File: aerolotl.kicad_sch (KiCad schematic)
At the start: 0 parts

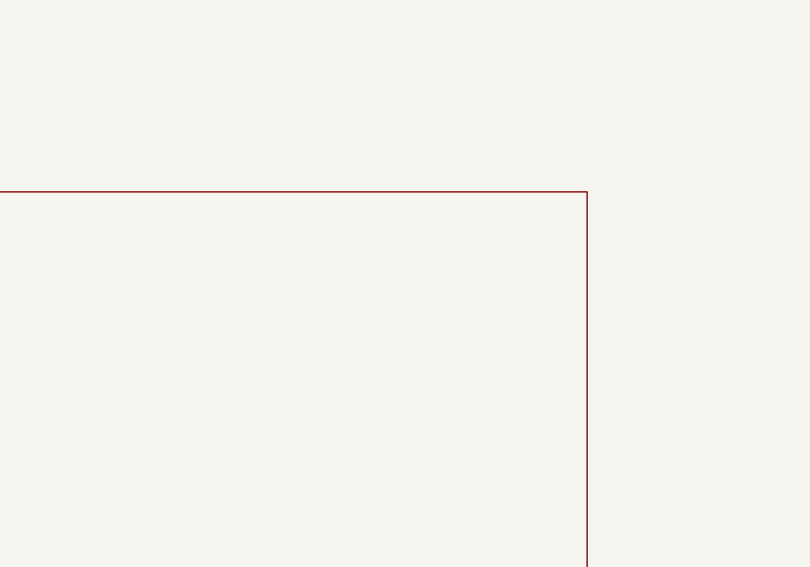
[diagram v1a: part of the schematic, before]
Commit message: Modified schematics for IMUs
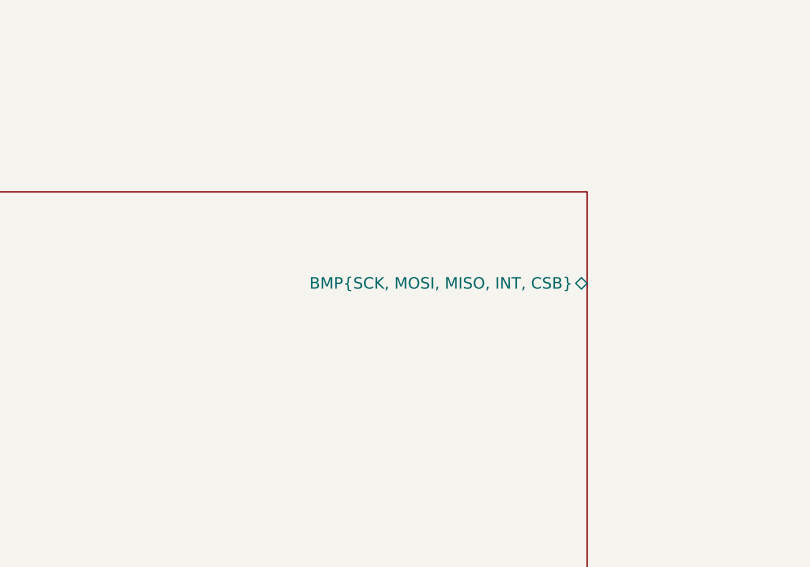
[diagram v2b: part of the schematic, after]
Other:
- sheet IMUs ports: added BMP{SCK, MOSI, MISO, INT, CSB}; removed none
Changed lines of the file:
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@@
+			)
+		)
+		(pin "BMP{SCK, MOSI, MISO, INT, CSB}" bidirectional
+			(at 104.14 218.44 0)
+			(effects
+				(font
+					(size 1.27 1.27)
+				)
+				(justify right)
 			)
 		)

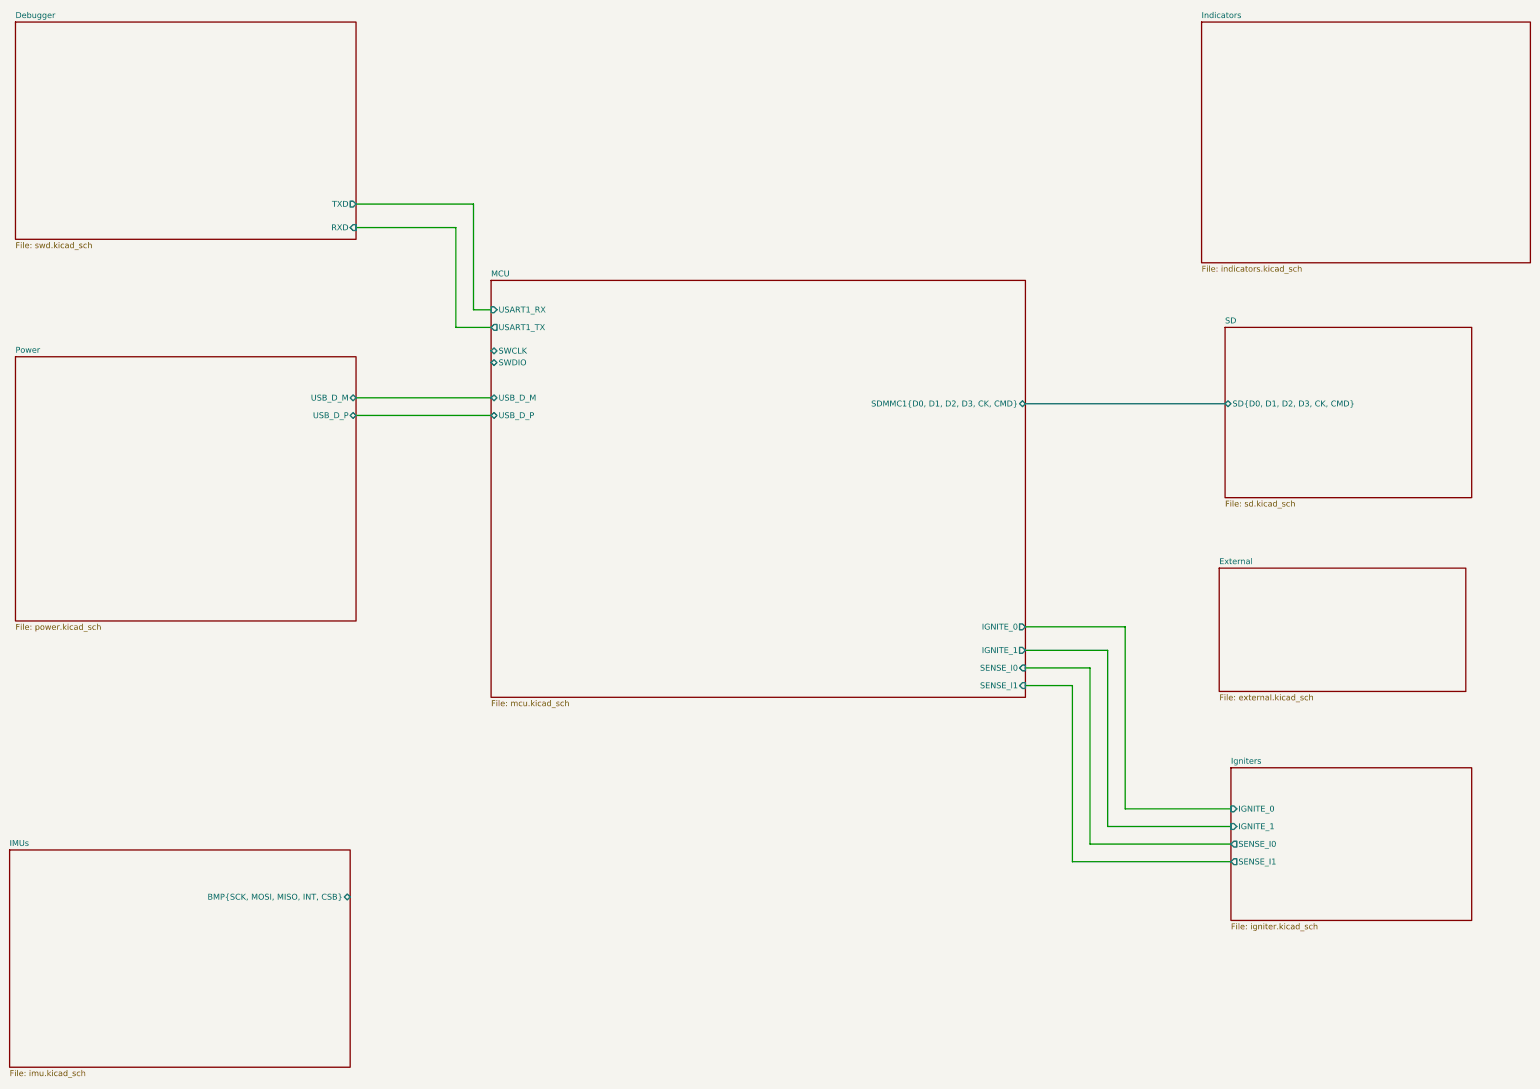
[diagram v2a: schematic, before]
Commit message: added current rush limiting resistors to bmp581
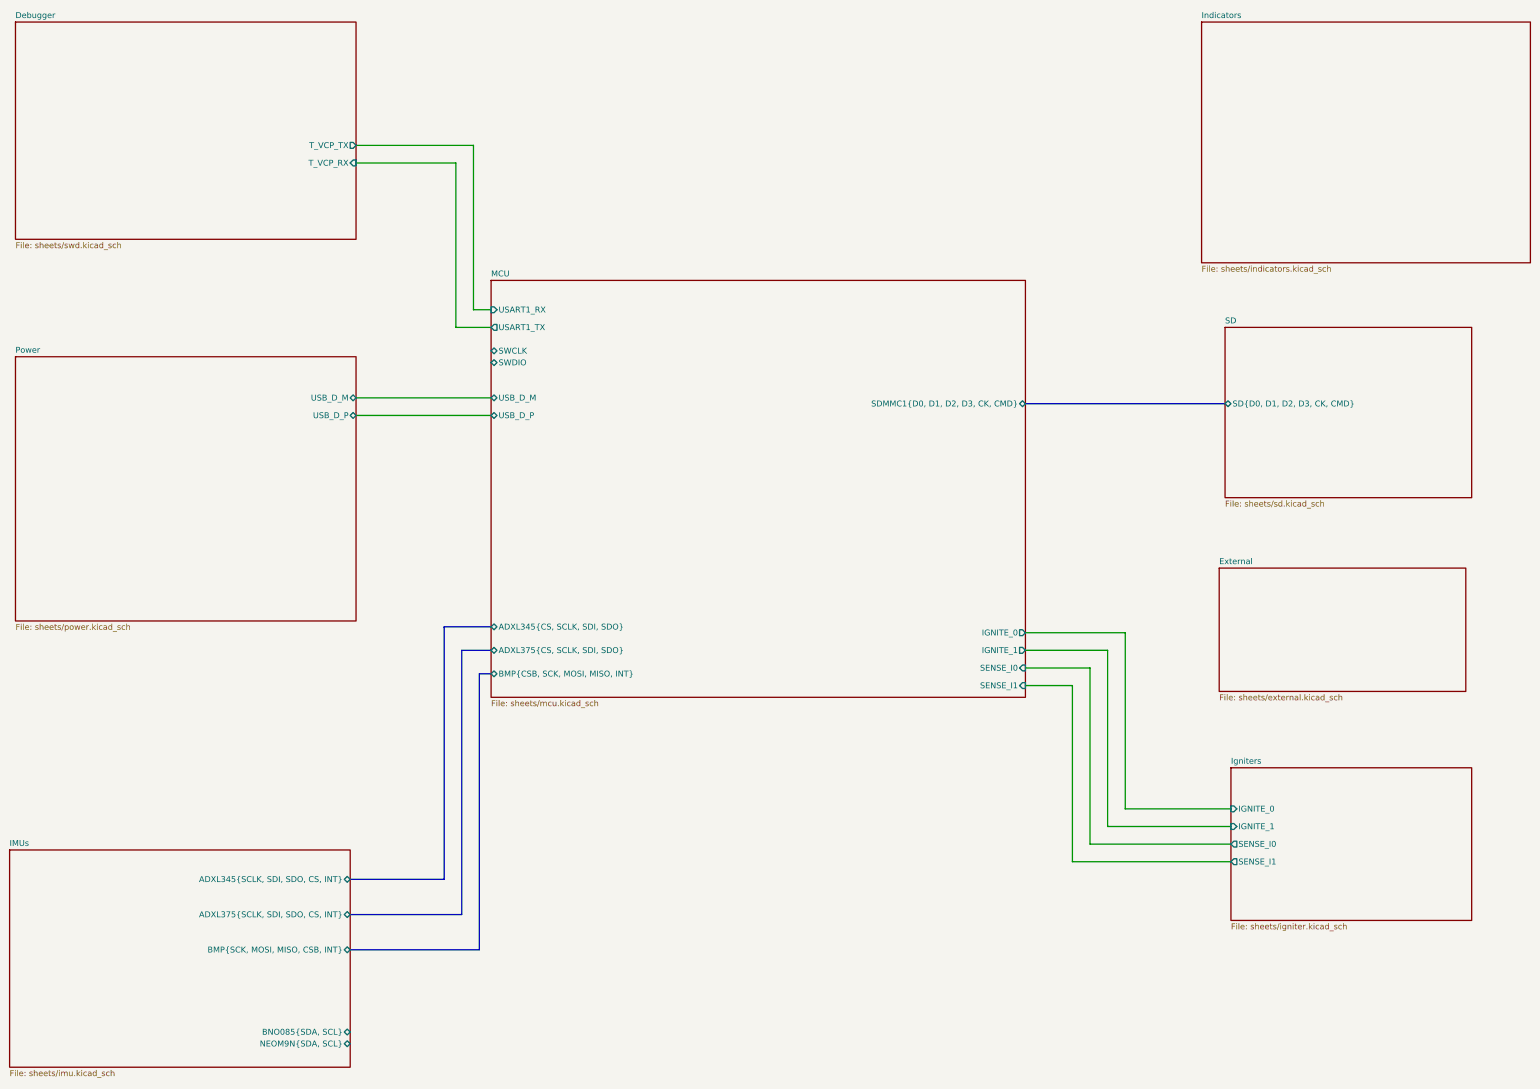
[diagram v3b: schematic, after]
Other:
- sheet Debugger: file swd.kicad_sch -> sheets/swd.kicad_sch
- sheet Debugger ports: added T_VCP_RX, T_VCP_TX; removed RXD, TXD
- sheet External: file external.kicad_sch -> sheets/external.kicad_sch
- sheet IMUs: file imu.kicad_sch -> sheets/imu.kicad_sch
- sheet IMUs ports: added ADXL345{SCLK, SDI, SDO, CS, INT}, ADXL375{SCLK, SDI, SDO, CS, INT}, BMP{SCK, MOSI, MISO, CSB, INT}, BNO085{SDA, SCL}, NEOM9N{SDA, SCL}; removed BMP{SCK, MOSI, MISO, INT, CSB}
- sheet Igniters: file igniter.kicad_sch -> sheets/igniter.kicad_sch
- sheet Indicators: file indicators.kicad_sch -> sheets/indicators.kicad_sch
- sheet MCU: file mcu.kicad_sch -> sheets/mcu.kicad_sch
- sheet MCU ports: added ADXL345{CS, SCLK, SDI, SDO}, ADXL375{CS, SCLK, SDI, SDO}, BMP{CSB, SCK, MOSI, MISO, INT}; removed none
- sheet Power: file power.kicad_sch -> sheets/power.kicad_sch
- sheet SD: file sd.kicad_sch -> sheets/sd.kicad_sch
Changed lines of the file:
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@@
 	(wire
 		(pts
-			(xy 271.78 160.02) (xy 271.78 199.39)
+			(xy 271.78 161.29) (xy 271.78 199.39)
 		)
 		(stroke
@@
 		)
 	)
-	(wire
-		(pts
-			(xy 250.19 160.02) (xy 271.78 160.02)
-		)
-		(stroke
-			(width 0)
-			(type default)
-		)
-	)
-	(wire
-		(pts
-			(xy 105.41 73.66) (xy 127 73.66)
+	(bus
+		(pts
+			(xy 104.14 214.63) (xy 124.46 214.63)
+		)
+		(stroke
+			(width 0)
+			(type default)
+		)
+	)
+	(bus
+		(pts
+			(xy 132.08 229.87) (xy 132.08 170.18)
+		)
+		(stroke
+			(width 0)
+			(type default)
+		)
+	)
+	(wire
+		(pts
+			(xy 250.19 161.29) (xy 271.78 161.29)
+		)
+		(stroke
+			(width 0)
+			(type default)
+		)
+	)
+	(wire
+		(pts
+			(xy 105.41 59.69) (xy 127 59.69)
 		)
 		(stroke
@@
 		)
 	)
-	(wire
-		(pts
-			(xy 105.41 68.58) (xy 130.81 68.58)
+	(bus
+		(pts
+			(xy 104.14 222.25) (xy 128.27 222.25)
+		)
+		(stroke
+			(width 0)
+			(type default)
+		)
+	)
+	(wire
+		(pts
+			(xy 105.41 55.88) (xy 130.81 55.88)
 		)
 		(stroke
@@
 		)
 	)
+	(bus
+		(pts
+			(xy 124.46 160.02) (xy 134.62 160.02)
+		)
+		(stroke
+			(width 0)
+			(type default)
+		)
+	)
+	(bus
+		(pts
+			(xy 128.27 222.25) (xy 128.27 165.1)
+		)
+		(stroke
+			(width 0)
+			(type default)
+		)
+	)
 	(wire
 		(pts
@@
 	(wire
 		(pts
-			(xy 130.81 68.58) (xy 130.81 91.44)
+			(xy 130.81 55.88) (xy 130.81 91.44)
+		)
+		(stroke
+			(width 0)
+			(type default)
+		)
+	)
+	(bus
+		(pts
+			(xy 132.08 170.18) (xy 134.62 170.18)
 		)
 		(stroke
@@
 		)
 	)
+	(bus
+		(pts
+			(xy 124.46 214.63) (xy 124.46 160.02)
+		)
+		(stroke
+			(width 0)
+			(type default)
+		)
+	)
+	(bus
+		(pts
+			(xy 104.14 229.87) (xy 132.08 229.87)
+		)
+		(stroke
+			(width 0)
+			(type default)
+		)
+	)
 	(wire
 		(pts
@@
 		)
 	)
-	(wire
-		(pts
-			(xy 127 73.66) (xy 127 95.25)
+	(bus
+		(pts
+			(xy 128.27 165.1) (xy 134.62 165.1)
+		)
+		(stroke
+			(width 0)
+			(type default)
+		)
+	)
+	(wire
+		(pts
+			(xy 127 59.69) (xy 127 95.25)
 		)
 		(stroke
@@
 			)
 		)
-		(property "Sheetfile" "swd.kicad_sch"
+		(property "Sheetfile" "sheets/swd.kicad_sch"
 			(at 31.75 76.7846 0)
 			(effects
@@
 			)
 		)
-		(pin "RXD" input
-			(at 105.41 73.66 0)
-			(effects
-				(font
-					(size 1.27 1.27)
-				)
-				(justify right)
-			)
-		)
-		(pin "TXD" output
-			(at 105.41 68.58 0)
+		(pin "T_VCP_RX" input
+			(at 105.41 59.69 0)
+			(effects
+				(font
+					(size 1.27 1.27)
+				)
+				(justify right)
+			)
+		)
+		(pin "T_VCP_TX" output
+			(at 105.41 55.88 0)
 			(effects
 				(font
@@
 			)
 		)
-		(property "Sheetfile" "sd.kicad_sch"
+		(property "Sheetfile" "sheets/sd.kicad_sch"
 			(at 293.37 132.6646 0)
 			(effects
@@
 			)
 		)
-		(property "Sheetfile" "igniter.kicad_sch"
+		(property "Sheetfile" "sheets/igniter.kicad_sch"
 			(at 294.64 224.1046 0)
 			(effects
@@
 			)
 		)
-		(property "Sheetfile" "external.kicad_sch"
+		(property "Sheetfile" "sheets/external.kicad_sch"
 			(at 292.1 174.5746 0)
 			(effects
@@
 			)
 		)
-		(property "Sheetfile" "indicators.kicad_sch"
+		(property "Sheetfile" "sheets/indicators.kicad_sch"
 			(at 288.29 81.8646 0)
 			(effects
@@
 			)
 		)
-		(property "Sheetfile" "power.kicad_sch"
+		(property "Sheetfile" "sheets/power.kicad_sch"
 			(at 31.75 159.3346 0)
 			(effects
@@
 			)
 		)
-		(property "Sheetfile" "imu.kicad_sch"
+		(property "Sheetfile" "sheets/imu.kicad_sch"
 			(at 30.48 255.8546 0)
 			(effects
@@
 			)
 		)
-		(pin "BMP{SCK, MOSI, MISO, INT, CSB}" bidirectional
-			(at 104.14 218.44 0)
+		(pin "ADXL345{SCLK, SDI, SDO, CS, INT}" bidirectional
+			(at 104.14 214.63 0)
+			(effects
+				(font
+					(size 1.27 1.27)
+				)
+				(justify right)
+			)
+		)
+		(pin "ADXL375{SCLK, SDI, SDO, CS, INT}" bidirectional
+			(at 104.14 222.25 0)
+			(effects
+				(font
+					(size 1.27 1.27)
+				)
+				(justify right)
+			)
+		)
+		(pin "BMP{SCK, MOSI, MISO, CSB, INT}" bidirectional
+			(at 104.14 229.87 0)
+			(effects
+				(font
+					(size 1.27 1.27)
+				)
+				(justify right)
+			)
+		)
+		(pin "BNO085{SDA, SCL}" bidirectional
+			(at 104.14 247.65 0)
+			(effects
+				(font
+					(size 1.27 1.27)
+				)
+				(justify right)
+			)
+		)
+		(pin "NEOM9N{SDA, SCL}" bidirectional
+			(at 104.14 250.19 0)
 			(effects
 				(font
@@
 			)
 		)
-		(property "Sheetfile" "mcu.kicad_sch"
+		(property "Sheetfile" "sheets/mcu.kicad_sch"
 			(at 134.62 175.8446 0)
 			(effects
@@
 		)
 		(pin "IGNITE_0" output
-			(at 250.19 160.02 0)
+			(at 250.19 161.29 0)
 			(effects
 				(font
@@
 			(effects
 				(font
+					(size 1.27 1.27)
+				)
+				(justify left)
+			)
+		)
+		(pin "ADXL345{CS, SCLK, SDI, SDO}" bidirectional
+			(at 134.62 160.02 180)
+			(effects
+				(font
+					(size 1.27 1.27)
+				)
+				(justify left)
+			)
+		)
+		(pin "ADXL375{CS, SCLK, SDI, SDO}" bidirectional
+			(at 134.62 165.1 180)
+			(effects
+				(font
+					(size 1.27 1.27)
+				)
+				(justify left)
+			)
+		)
+		(pin "BMP{CSB, SCK, MOSI, MISO, INT}" bidirectional
+			(at 134.62 170.18 180)
+			(effects
+				(font

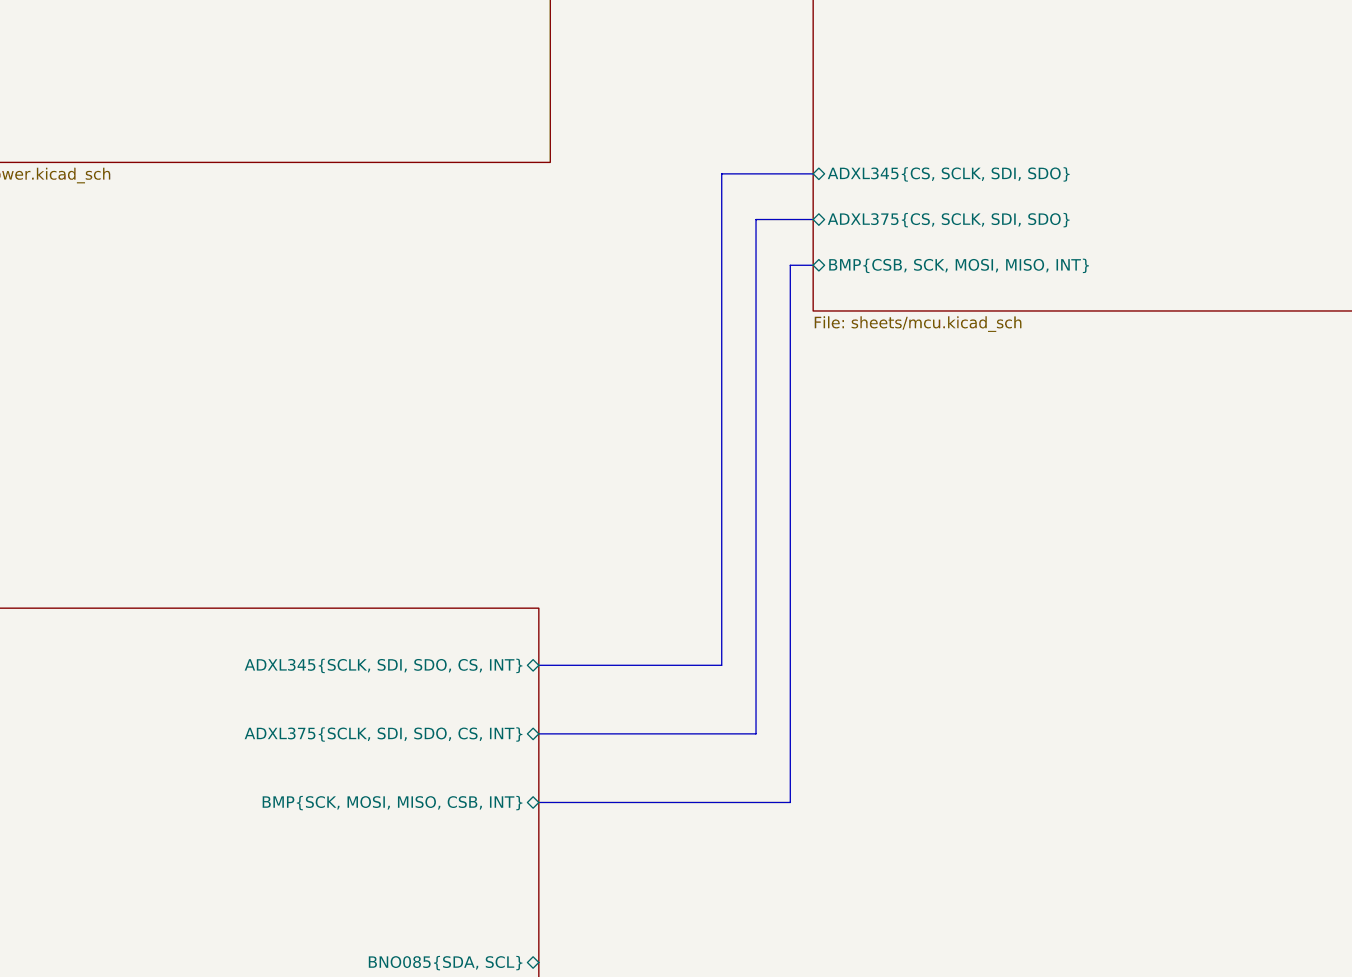
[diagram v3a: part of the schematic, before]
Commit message: Added NEOM9N breakout symbol
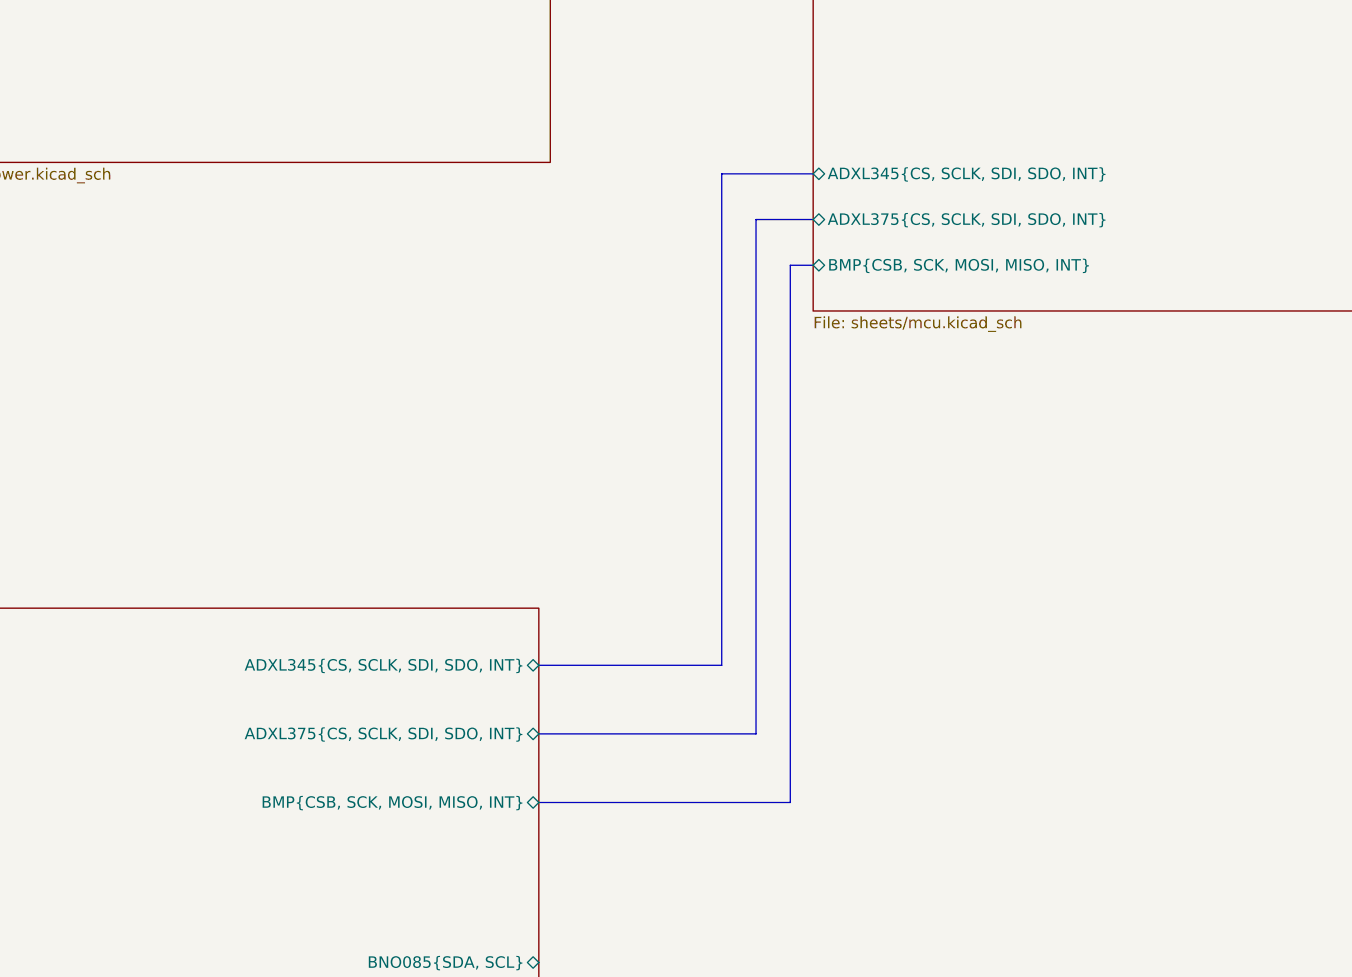
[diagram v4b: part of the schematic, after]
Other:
- sheet IMUs ports: added ADXL345{CS, SCLK, SDI, SDO, INT}, ADXL375{CS, SCLK, SDI, SDO, INT}, BMP{CSB, SCK, MOSI, MISO, INT}; removed ADXL345{SCLK, SDI, SDO, CS, INT}, ADXL375{SCLK, SDI, SDO, CS, INT}, BMP{SCK, MOSI, MISO, CSB, INT}
- sheet MCU ports: added ADXL345{CS, SCLK, SDI, SDO, INT}, ADXL375{CS, SCLK, SDI, SDO, INT}; removed ADXL345{CS, SCLK, SDI, SDO}, ADXL375{CS, SCLK, SDI, SDO}
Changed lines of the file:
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@@
-			)
-		)
-		(pin "ADXL345{SCLK, SDI, SDO, CS, INT}" bidirectional
-			(at 104.14 214.63 0)
-			(effects
-				(font
-					(size 1.27 1.27)
-				)
-				(justify right)
-			)
-		)
-		(pin "ADXL375{SCLK, SDI, SDO, CS, INT}" bidirectional
-			(at 104.14 222.25 0)
-			(effects
-				(font
-					(size 1.27 1.27)
-				)
-				(justify right)
-			)
-		)
-		(pin "BMP{SCK, MOSI, MISO, CSB, INT}" bidirectional
-			(at 104.14 229.87 0)
-			(effects
-				(font
-					(size 1.27 1.27)
-				)
-				(justify right)
 			)
 		)
@@
 		(pin "NEOM9N{SDA, SCL}" bidirectional
 			(at 104.14 250.19 0)
+			(effects
+				(font
+					(size 1.27 1.27)
+				)
+				(justify right)
+			)
+		)
+		(pin "ADXL345{CS, SCLK, SDI, SDO, INT}" bidirectional
+			(at 104.14 214.63 0)
+			(effects
+				(font
+					(size 1.27 1.27)
+				)
+				(justify right)
+			)
+		)
+		(pin "ADXL375{CS, SCLK, SDI, SDO, INT}" bidirectional
+			(at 104.14 222.25 0)
+			(effects
+				(font
+					(size 1.27 1.27)
+				)
+				(justify right)
+			)
+		)
+		(pin "BMP{CSB, SCK, MOSI, MISO, INT}" bidirectional
+			(at 104.14 229.87 0)
 			(effects
 				(font
@@
 			)
 		)
-		(pin "ADXL345{CS, SCLK, SDI, SDO}" bidirectional
-			(at 134.62 160.02 180)
-			(effects
-				(font
-					(size 1.27 1.27)
-				)
-				(justify left)
-			)
-		)
-		(pin "ADXL375{CS, SCLK, SDI, SDO}" bidirectional
-			(at 134.62 165.1 180)
-			(effects
-				(font
-					(size 1.27 1.27)
-				)
-				(justify left)
-			)
-		)
 		(pin "BMP{CSB, SCK, MOSI, MISO, INT}" bidirectional
 			(at 134.62 170.18 180)
 			(effects
 				(font
+					(size 1.27 1.27)
+				)
+				(justify left)
+			)
+		)
+		(pin "ADXL345{CS, SCLK, SDI, SDO, INT}" bidirectional
+			(at 134.62 160.02 180)
+			(effects
+				(font
+					(size 1.27 1.27)
+				)
+				(justify left)
+			)
+		)
+		(pin "ADXL375{CS, SCLK, SDI, SDO, INT}" bidirectional
+			(at 134.62 165.1 180)
+			(effects
+				(font
